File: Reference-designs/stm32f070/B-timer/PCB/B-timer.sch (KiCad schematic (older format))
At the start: 121 parts, among them J1 USB_B_Micro, J2 Conn_02x05_Odd_Even, SW1 SW_Push, SW2 SW_Push, SW3 SW_Push, U1 STM32F070C6Tx, U2 MIC5504-3.3YM5

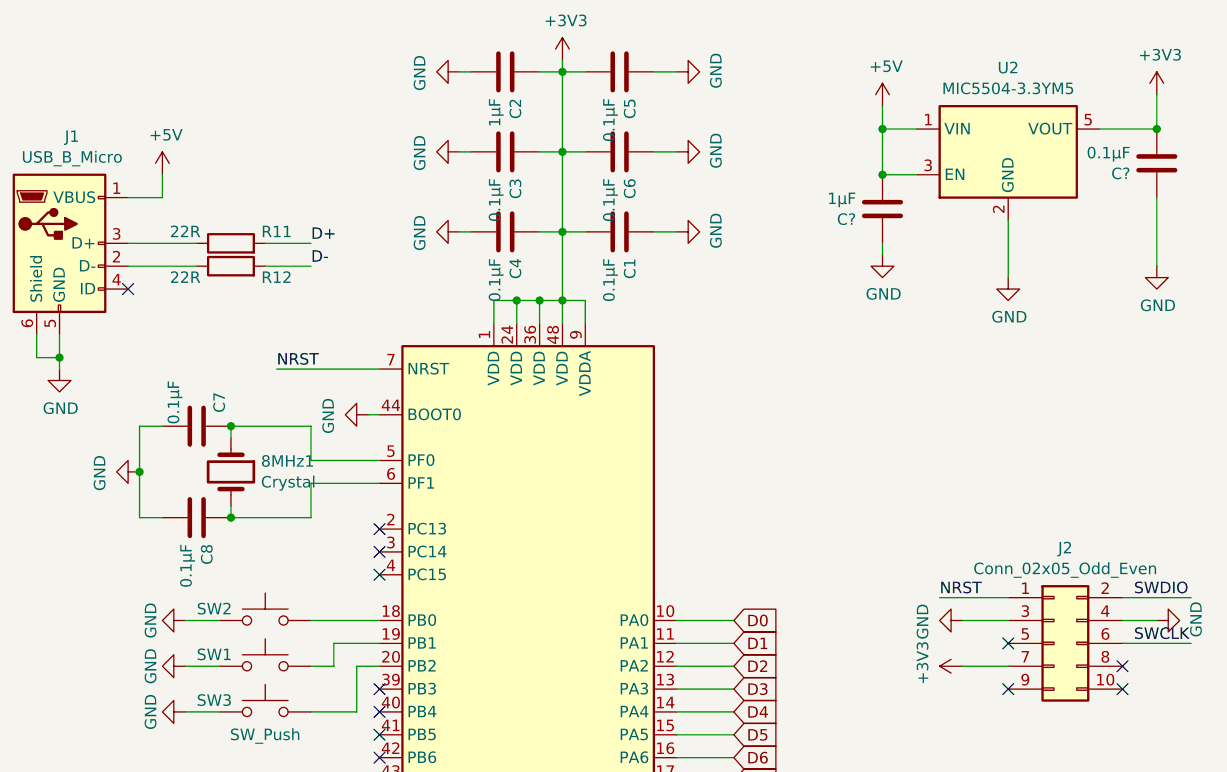
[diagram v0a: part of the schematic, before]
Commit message: Generated code for B-timer V2
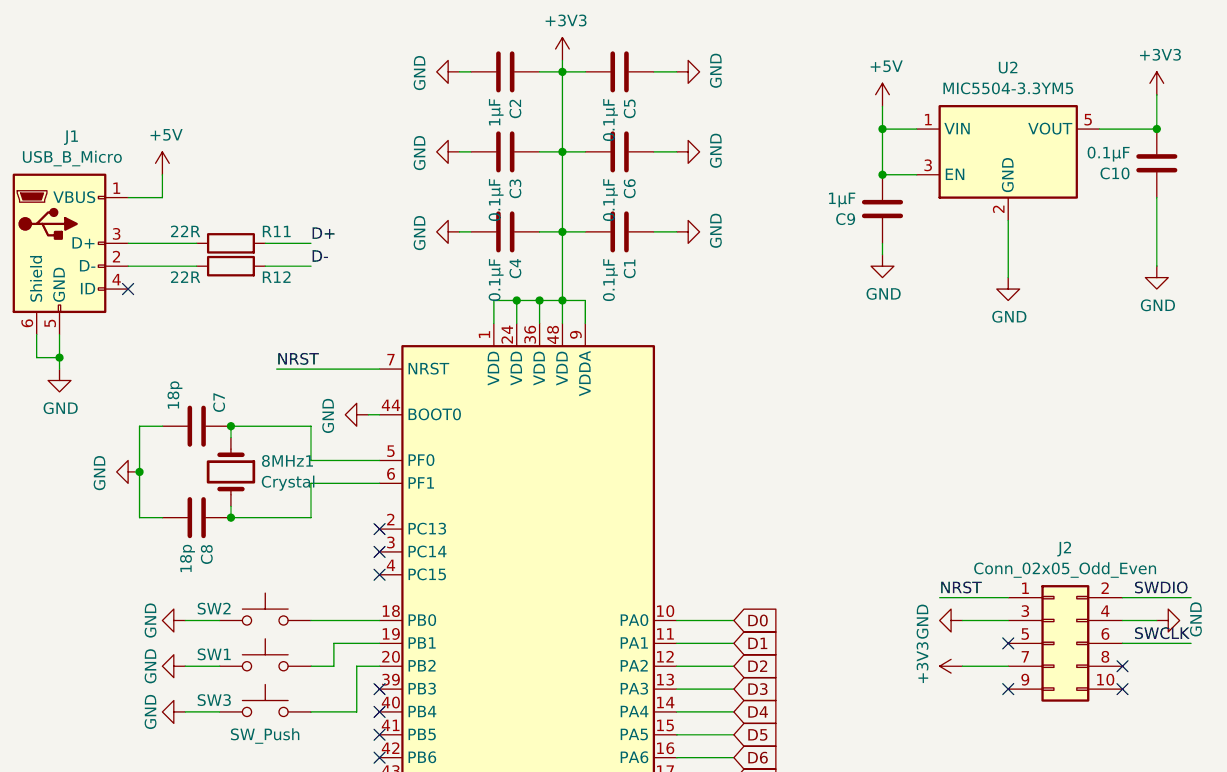
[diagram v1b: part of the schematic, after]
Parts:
- 8MHz1: MPN (none) -> FC4SDCBMF8.0-T1
- C7, C8: value 0.1µF -> 18p
- J2: MPN (none) -> 0015912100
- U2: MPN (none) -> MIC5501-3.0YM5-TR
- gave numbers to parts that had none: 2
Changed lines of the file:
@@
 F 2 "Package_TO_SOT_SMD:SOT-23-5" H 10100 1300 50  0001 C CNN
 F 3 "http://ww1.microchip.com/downloads/en/DeviceDoc/MIC550X.pdf" H 9850 1950 50  0001 C CNN
+F 4 "MIC5501-3.0YM5-TR" H 10100 1700 50  0001 C CNN "MPN"
 	1    10100 1700
 	1    0    0    -1
@@
 F 2 "Crystal:Crystal_SMD_HC49-SD" H 6700 3100 50  0001 C CNN
 F 3 "~" H 6700 3100 50  0001 C CNN
+F 4 "FC4SDCBMF8.0-T1" V 6700 3100 50  0001 C CNN "MPN"
 	1    6700 3100
 	0    1    1    0
@@
 P 6550 2900
 F 0 "C7" H 6400 3000 50  0000 L CNN
-F 1 "0.1µF" H 6350 2800 50  0000 L CNN
+F 1 "18p" H 6350 2800 50  0000 L CNN
 F 2 "Capacitor_SMD:C_0402_1005Metric" H 6588 2750 50  0001 C CNN
 F 3 "~" H 6550 2900 50  0001 C CNN
@@
 P 6550 3300
 F 0 "C8" H 6665 3346 50  0000 L CNN
-F 1 "0.1µF" H 6665 3255 50  0000 L CNN
+F 1 "18p" H 6665 3255 50  0000 L CNN
 F 2 "Capacitor_SMD:C_0402_1005Metric" H 6588 3150 50  0001 C CNN
 F 3 "~" H 6550 3300 50  0001 C CNN
@@
 F 2 "Connector_PinHeader_2.54mm:PinHeader_2x05_P2.54mm_Vertical_SMD" H 10300 3850 50  0001 C CNN
 F 3 "~" H 10300 3850 50  0001 C CNN
+F 4 "0015912100" H 10300 3850 50  0001 C CNN "MPN"
 	1    10300 3850
 	1    0    0    -1
@@
 	8150 1300 8150 1350
 $Comp
-L Device:C C?
+L Device:C C9
 U 1 1 5EB2BE10
 P 9550 1950
-F 0 "C?" H 9665 1996 50  0000 L CNN
+F 0 "C9" H 9665 1996 50  0000 L CNN
 F 1 "1µF" H 9665 1905 50  0000 L CNN
 F 2 "Capacitor_SMD:C_0402_1005Metric" H 9588 1800 50  0001 C CNN
@@
 Connection ~ 9550 1800
 $Comp
-L power:GND #PWR?
+L power:GND #PWR02
 U 1 1 5EB2C0B0
 P 9550 2150
-F 0 "#PWR?" H 9550 1900 50  0001 C CNN
+F 0 "#PWR02" H 9550 1900 50  0001 C CNN
 F 1 "GND" H 9555 1977 50  0000 C CNN
 F 2 "" H 9550 2150 50  0001 C CNN
@@
 	9550 2100 9550 2150
 $Comp
-L Device:C C?
+L Device:C C10
 U 1 1 5EB7B655
 P 10750 1750
-F 0 "C?" H 10865 1796 50  0000 L CNN
+F 0 "C10" H 10865 1796 50  0000 L CNN
 F 1 "0.1µF" H 10865 1705 50  0000 L CNN
 F 2 "Capacitor_SMD:C_0402_1005Metric" H 10788 1600 50  0001 C CNN
@@
 Connection ~ 10750 1600
 $Comp
-L power:GND #PWR?
+L power:GND #PWR04
 U 1 1 5EB7B7FE
 P 10750 2200
-F 0 "#PWR?" H 10750 1950 50  0001 C CNN
+F 0 "#PWR04" H 10750 1950 50  0001 C CNN
 F 1 "GND" H 10755 2027 50  0000 C CNN
 F 2 "" H 10750 2200 50  0001 C CNN

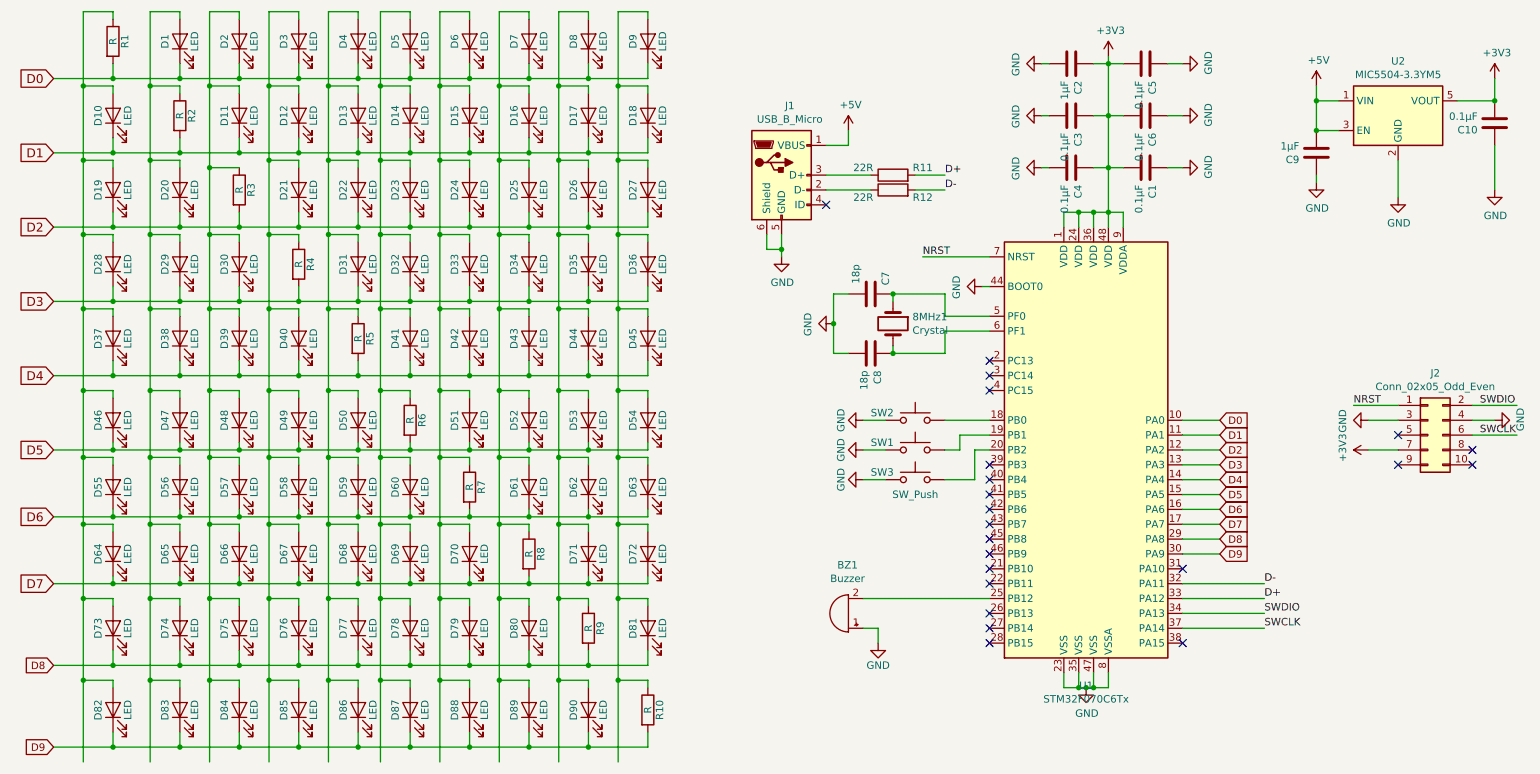
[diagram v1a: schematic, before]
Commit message: Adjusted 68R and 18pF values and regenerated kicad_pcb file
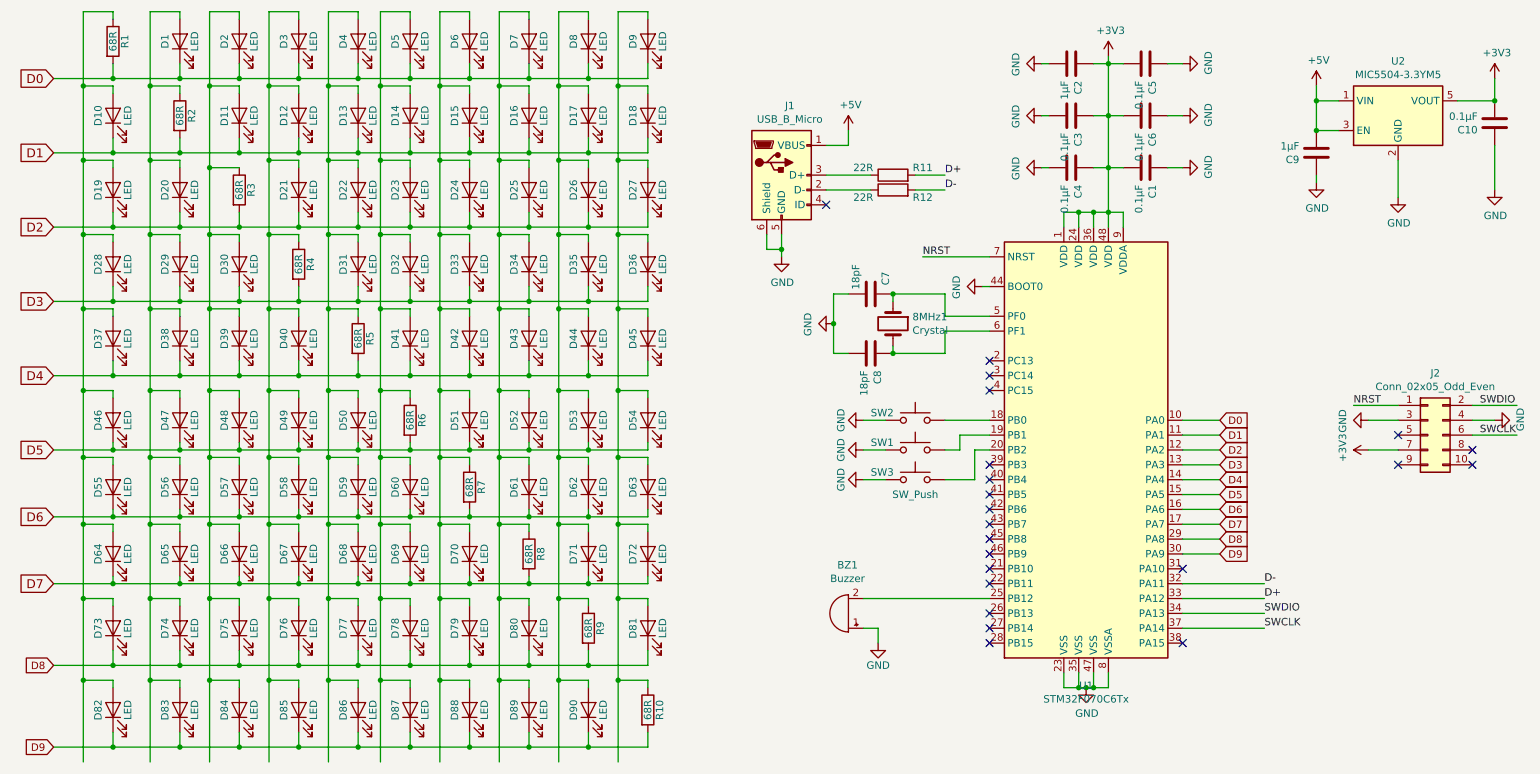
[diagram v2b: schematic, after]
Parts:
- C7, C8: value 18p -> 18pF
- R1, R10, R2, R3, R4, R5, R6, R7, R8, R9: value R -> 68R
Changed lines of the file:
@@
 P 1450 1200
 F 0 "R1" V 1530 1200 50  0000 C CNN
-F 1 "R" V 1450 1200 50  0000 C CNN
+F 1 "68R" V 1450 1200 50  0000 C CNN
 F 2 "Resistors_SMD:R_0402" V 1380 1200 50  0001 C CNN
 F 3 "" H 1450 1200 50  0000 C CNN
@@
 P 1900 1700
 F 0 "R2" V 1980 1700 50  0000 C CNN
-F 1 "R" V 1900 1700 50  0000 C CNN
+F 1 "68R" V 1900 1700 50  0000 C CNN
 F 2 "Resistors_SMD:R_0402" V 1830 1700 50  0001 C CNN
 F 3 "" H 1900 1700 50  0000 C CNN
@@
 P 2300 2200
 F 0 "R3" V 2380 2200 50  0000 C CNN
-F 1 "R" V 2300 2200 50  0000 C CNN
+F 1 "68R" V 2300 2200 50  0000 C CNN
 F 2 "Resistors_SMD:R_0402" V 2230 2200 50  0001 C CNN
 F 3 "" H 2300 2200 50  0000 C CNN
@@
 P 2700 2700
 F 0 "R4" V 2780 2700 50  0000 C CNN
-F 1 "R" V 2700 2700 50  0000 C CNN
+F 1 "68R" V 2700 2700 50  0000 C CNN
 F 2 "Resistors_SMD:R_0402" V 2630 2700 50  0001 C CNN
 F 3 "" H 2700 2700 50  0000 C CNN
@@
 P 3100 3200
 F 0 "R5" V 3180 3200 50  0000 C CNN
-F 1 "R" V 3100 3200 50  0000 C CNN
+F 1 "68R" V 3100 3200 50  0000 C CNN
 F 2 "Resistors_SMD:R_0402" V 3030 3200 50  0001 C CNN
 F 3 "" H 3100 3200 50  0000 C CNN
@@
 P 3450 3750
 F 0 "R6" V 3530 3750 50  0000 C CNN
-F 1 "R" V 3450 3750 50  0000 C CNN
+F 1 "68R" V 3450 3750 50  0000 C CNN
 F 2 "Resistors_SMD:R_0402" V 3380 3750 50  0001 C CNN
 F 3 "" H 3450 3750 50  0000 C CNN
@@
 P 3850 4200
 F 0 "R7" V 3930 4200 50  0000 C CNN
-F 1 "R" V 3850 4200 50  0000 C CNN
+F 1 "68R" V 3850 4200 50  0000 C CNN
 F 2 "Resistors_SMD:R_0402" V 3780 4200 50  0001 C CNN
 F 3 "" H 3850 4200 50  0000 C CNN
@@
 P 4250 4650
 F 0 "R8" V 4330 4650 50  0000 C CNN
-F 1 "R" V 4250 4650 50  0000 C CNN
+F 1 "68R" V 4250 4650 50  0000 C CNN
 F 2 "Resistors_SMD:R_0402" V 4180 4650 50  0001 C CNN
 F 3 "" H 4250 4650 50  0000 C CNN
@@
 P 4650 5150
 F 0 "R9" V 4730 5150 50  0000 C CNN
-F 1 "R" V 4650 5150 50  0000 C CNN
+F 1 "68R" V 4650 5150 50  0000 C CNN
 F 2 "Resistors_SMD:R_0402" V 4580 5150 50  0001 C CNN
 F 3 "" H 4650 5150 50  0000 C CNN
@@
 P 5050 5700
 F 0 "R10" V 5130 5700 50  0000 C CNN
-F 1 "R" V 5050 5700 50  0000 C CNN
+F 1 "68R" V 5050 5700 50  0000 C CNN
 F 2 "Resistors_SMD:R_0402" V 4980 5700 50  0001 C CNN
 F 3 "" H 5050 5700 50  0000 C CNN
@@
 P 6550 2900
 F 0 "C7" H 6400 3000 50  0000 L CNN
-F 1 "18p" H 6350 2800 50  0000 L CNN
+F 1 "18pF" H 6350 2800 50  0000 L CNN
 F 2 "Capacitor_SMD:C_0402_1005Metric" H 6588 2750 50  0001 C CNN
 F 3 "~" H 6550 2900 50  0001 C CNN
@@
 P 6550 3300
 F 0 "C8" H 6665 3346 50  0000 L CNN
-F 1 "18p" H 6665 3255 50  0000 L CNN
+F 1 "18pF" H 6665 3255 50  0000 L CNN
 F 2 "Capacitor_SMD:C_0402_1005Metric" H 6588 3150 50  0001 C CNN
 F 3 "~" H 6550 3300 50  0001 C CNN
